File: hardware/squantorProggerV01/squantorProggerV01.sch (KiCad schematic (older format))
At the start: 4 parts

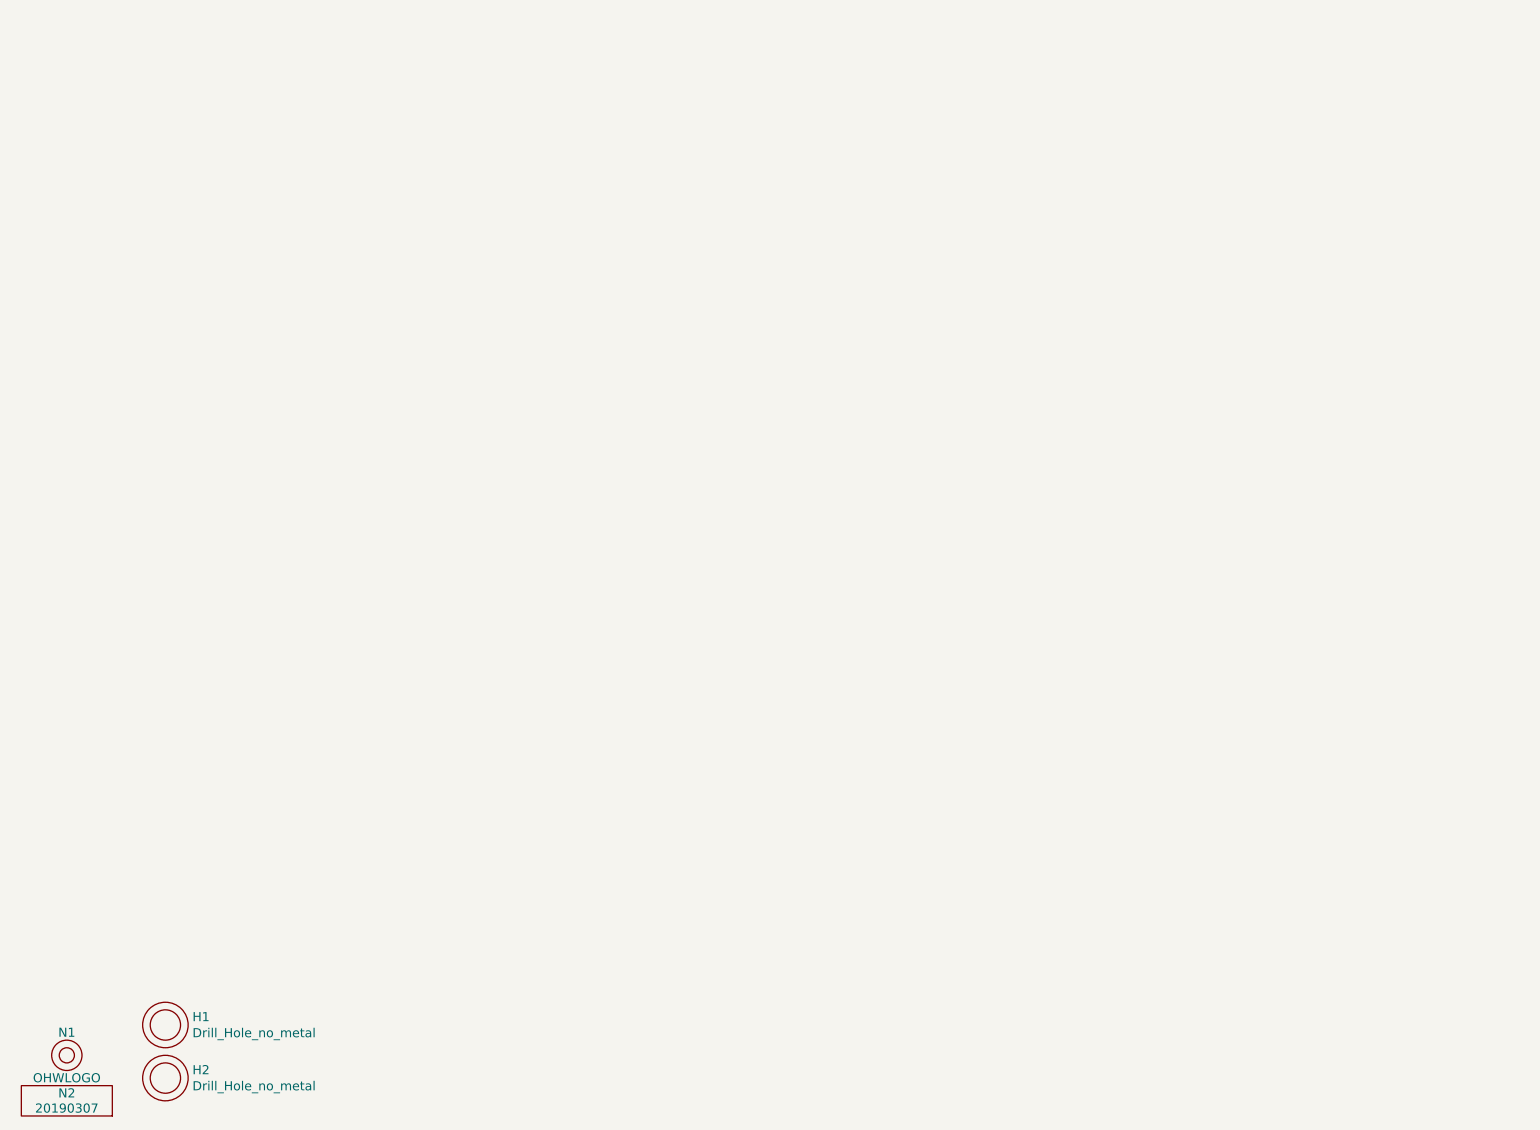
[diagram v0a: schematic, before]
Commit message: placed connectors
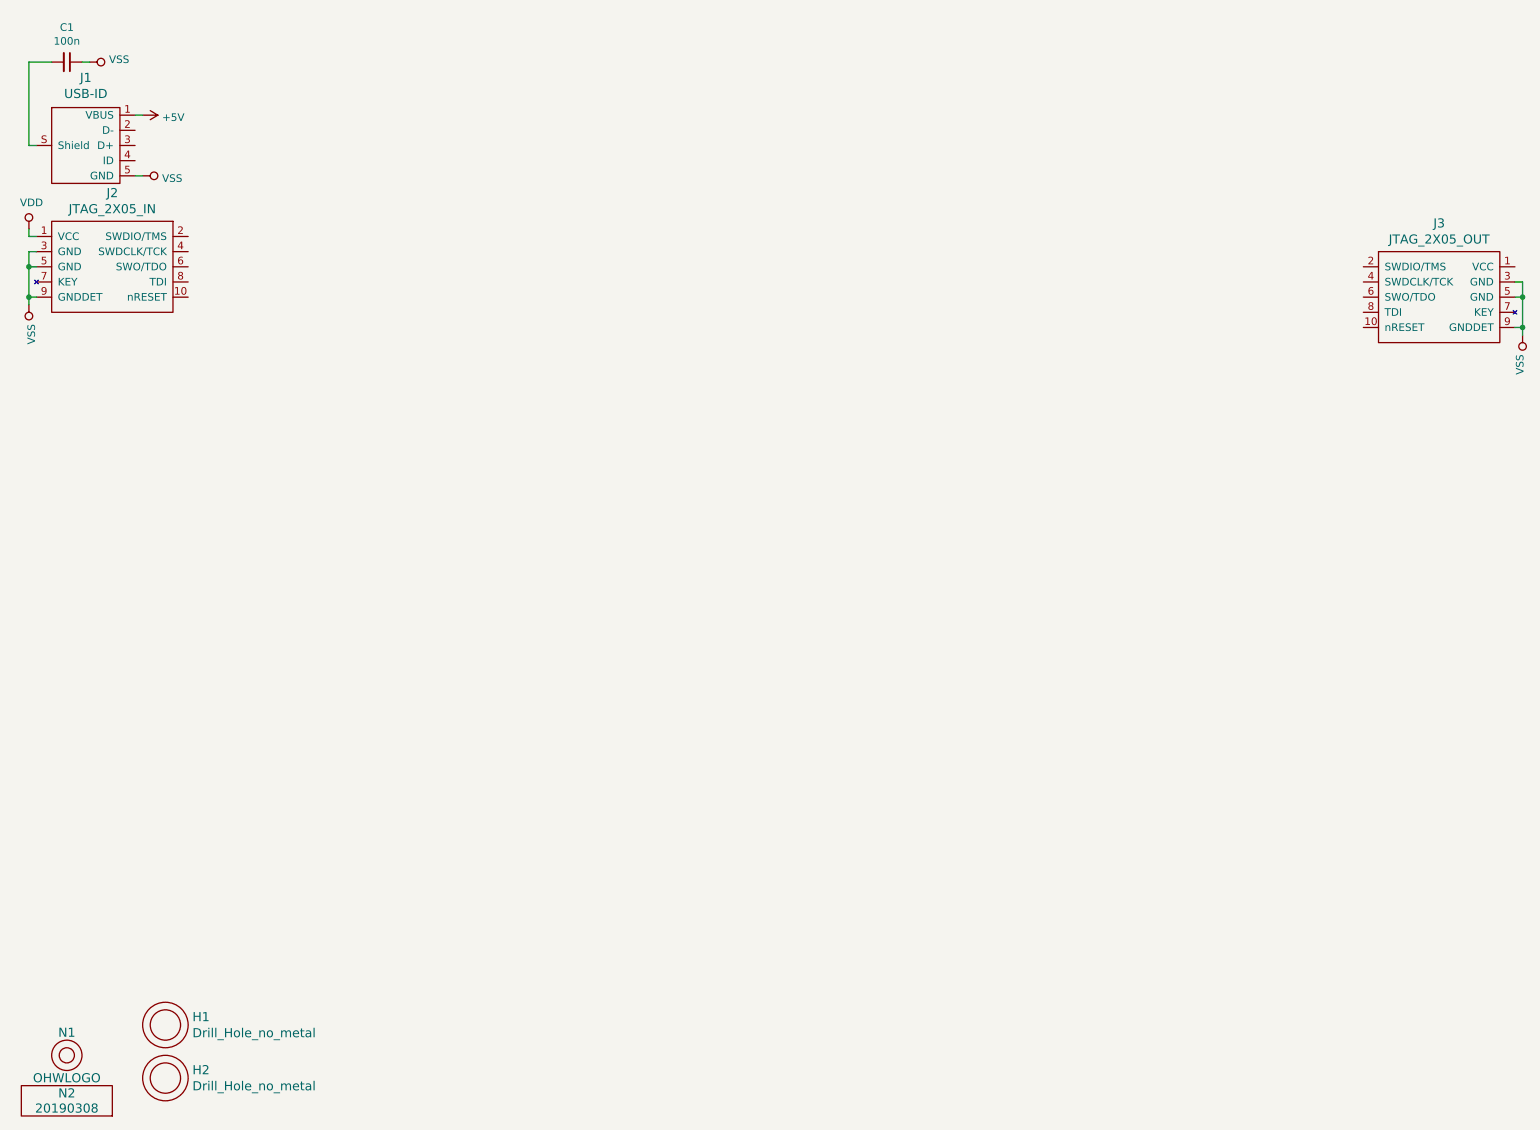
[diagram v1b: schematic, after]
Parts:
- added C1: 100n, SquantorRcl:C_0805, symbol Device:C_Small
- added J1: USB-ID, SquantorUsb:USB-muB-SMD_TH, symbol SquantorUsb:USB-ID
- added J2: JTAG_2X05_IN, SquantorConnectors:Header-0127-2X05-H006, symbol SquantorConnectors:JTAG_2X05_IN
- added J3: JTAG_2X05_OUT, SquantorConnectors:Header-Shr-0127-2X05-H006, symbol SquantorConnectors:JTAG_2X05_OUT
- N2: value 20190307 -> 20190308
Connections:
- new net: C1.2, J1.S (Shield)
- new net +5V: J1.1 (VBUS)
- new net VDD: J2.1 (VCC)
- new net VSS: C1.1, J1.5 (GND), J2.3 (GND), J2.5 (GND), J2.9 (GNDDET), J3.3 (GND), J3.5 (GND), J3.9 (GNDDET)
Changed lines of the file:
@@
 EESchema Schematic File Version 4
-LIBS:Hammond_1551M_OSH2layer-cache
+LIBS:squantorProggerV01-cache
 EELAYER 26 0
 EELAYER END
@@
 P 850 7700
 F 0 "N2" H 850 7800 60  0000 C CNN
-F 1 "20190307" H 850 7700 60  0000 C CNN
+F 1 "20190308" H 850 7700 60  0000 C CNN
 F 2 "SquantorLabels:Label_version" H 850 7700 60  0001 C CNN
 F 3 "" H 850 7700 60  0001 C CNN
@@
 	1    0    0    -1
 $EndComp
+$Comp
+L SquantorUsb:USB-ID J1
+U 1 1 5C82E08A
+P 950 1350
+F 0 "J1" H 975 1797 60  0000 C CNN
+F 1 "USB-ID" H 975 1691 60  0000 C CNN
+F 2 "SquantorUsb:USB-muB-SMD_TH" H 1100 1400 60  0001 C CNN
+F 3 "" H 1100 1400 60  0001 C CNN
+	1    950  1350
+	1    0    0    -1
+$EndComp
+$Comp
+L SquantorConnectors:JTAG_2X05_IN J2
+U 1 1 5C82F4B4
+P 1150 2150
+F 0 "J2" H 1150 2637 60  0000 C CNN
+F 1 "JTAG_2X05_IN" H 1150 2531 60  0000 C CNN
+F 2 "SquantorConnectors:Header-0127-2X05-H006" H 1150 2300 60  0001 C CNN
+F 3 "" H 1150 2300 60  0001 C CNN
+	1    1150 2150
+	-1   0    0    -1
+$EndComp
+$Comp
+L SquantorConnectors:JTAG_2X05_OUT J3
+U 1 1 5C82F5E3
+P 9900 2350
+F 0 "J3" H 9900 2837 60  0000 C CNN
+F 1 "JTAG_2X05_OUT" H 9900 2731 60  0000 C CNN
+F 2 "SquantorConnectors:Header-Shr-0127-2X05-H006" H 9900 2500 60  0001 C CNN
+F 3 "" H 9900 2500 60  0001 C CNN
+	1    9900 2350
+	1    0    0    -1
+$EndComp
+$Comp
+L power:VSS #PWR0101
+U 1 1 5C82FAFA
+P 1350 1550
+F 0 "#PWR0101" H 1350 1400 50  0001 C CNN
+F 1 "VSS" V 1367 1678 50  0000 L CNN
+F 2 "" H 1350 1550 50  0001 C CNN
+F 3 "" H 1350 1550 50  0001 C CNN
+	1    1350 1550
+	0    1    1    0
+$EndComp
+$Comp
+L power:VSS #PWR0102
+U 1 1 5C82FB3D
+P 600 2400
+F 0 "#PWR0102" H 600 2250 50  0001 C CNN
+F 1 "VSS" V 617 2528 50  0000 L CNN
+F 2 "" H 600 2400 50  0001 C CNN
+F 3 "" H 600 2400 50  0001 C CNN
+	1    600  2400
+	1    0    0    1
+$EndComp
+$Comp
+L power:VSS #PWR0103
+U 1 1 5C82FB56
+P 10450 2600
+F 0 "#PWR0103" H 10450 2450 50  0001 C CNN
+F 1 "VSS" V 10467 2728 50  0000 L CNN
+F 2 "" H 10450 2600 50  0001 C CNN
+F 3 "" H 10450 2600 50  0001 C CNN
+	1    10450 2600
+	-1   0    0    1
+$EndComp
+Wire Wire Line
+	10400 2250 10450 2250
+Wire Wire Line
+	10450 2250 10450 2350
+Wire Wire Line
+	10450 2350 10450 2550
+Wire Wire Line
+	10450 2550 10400 2550
+Connection ~ 10450 2350
+Wire Wire Line
+	10400 2350 10450 2350
+Wire Wire Line
+	650  2050 600  2050
+Wire Wire Line
+	600  2050 600  2150
+Wire Wire Line
+	650  2150 600  2150
+Connection ~ 600  2150
+Wire Wire Line
+	650  2350 600  2350
+Wire Wire Line
+	600  2350 600  2150
+Wire Wire Line
+	1300 1550 1350 1550
+Wire Wire Line
+	600  2400 600  2350
+Connection ~ 600  2350
+Wire Wire Line
+	10450 2600 10450 2550
+Connection ~ 10450 2550
+Wire Wire Line
+	650  1950 600  1950
+Wire Wire Line
+	600  1950 600  1900
+$Comp
+L Device:C_Small C1
+U 1 1 5C830A08
+P 850 800
+F 0 "C1" V 621 800 50  0000 C CNN
+F 1 "100n" V 712 800 50  0000 C CNN
+F 2 "SquantorRcl:C_0805" H 850 800 50  0001 C CNN
+F 3 "~" H 850 800 50  0001 C CNN
+	1    850  800
+	0    1    1    0
+$EndComp
+$Comp
+L power:VDD #PWR0104
+U 1 1 5C830AEB
+P 600 1900
+F 0 "#PWR0104" H 600 1750 50  0001 C CNN
+F 1 "VDD" H 617 2073 50  0000 C CNN
+F 2 "" H 600 1900 50  0001 C CNN
+F 3 "" H 600 1900 50  0001 C CNN
+	1    600  1900
+	1    0    0    -1
+$EndComp
+$Comp
+L power:VSS #PWR0105
+U 1 1 5C830B0D
+P 1000 800
+F 0 "#PWR0105" H 1000 650 50  0001 C CNN
+F 1 "VSS" V 1017 928 50  0000 L CNN
+F 2 "" H 1000 800 50  0001 C CNN
+F 3 "" H 1000 800 50  0001 C CNN
+	1    1000 800
+	0    1    -1   0
+$EndComp
+Wire Wire Line
+	650  1350 600  1350
+Wire Wire Line
+	600  1350 600  800
+Wire Wire Line
+	600  800  750  800
+Wire Wire Line
+	1000 800  950  800
+$Comp
+L power:+5V #PWR0106
+U 1 1 5C8314E9
+P 1350 1150
+F 0 "#PWR0106" H 1350 1000 50  0001 C CNN
+F 1 "+5V" V 1365 1278 50  0000 L CNN
+F 2 "" H 1350 1150 50  0001 C CNN
+F 3 "" H 1350 1150 50  0001 C CNN
+	1    1350 1150
+	0    1    1    0
+$EndComp
+Wire Wire Line
+	1300 1150 1350 1150
 $EndSCHEMATC

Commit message: newer Pcb library, started usb serial bits
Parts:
- added C?: 1u, SquantorRcl:C_0603, symbol Device:C_Small
- added U?: CH340E, symbol SquantorWCH:CH340E
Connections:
- net +5V: now also U?.7 (VCC)
- net VSS: now also C?.2, U?.3 (GND)
- net USB_D-: now reaches J1.2 (D-)
- net USB_D-: now also U?.2 (UD-)
- net USB_D+: now reaches J1.3 (D+)
- net USB_D+: now also U?.1 (UD+)
- new net: C?.1, U?.10 (V3)
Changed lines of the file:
@@
 Wire Wire Line
 	1300 1150 1350 1150
+$Comp
+L SquantorWCH:CH340E U?
+U 1 1 5C83DAAF
+P 2600 1350
+F 0 "U?" H 2600 1815 50  0000 C CNN
+F 1 "CH340E" H 2600 1724 50  0000 C CNN
+F 2 "" H 2600 1250 50  0001 C CNN
+F 3 "" H 2600 1250 50  0001 C CNN
+	1    2600 1350
+	1    0    0    -1
+$EndComp
+Wire Wire Line
+	1300 1250 1450 1250
+Wire Wire Line
+	1300 1350 1450 1350
+Text Label 1450 1250 0    50   ~ 0
+USB_D-
+Text Label 1450 1350 0    50   ~ 0
+USB_D+
+$Comp
+L power:VSS #PWR?
+U 1 1 5C83E568
+P 2200 1350
+F 0 "#PWR?" H 2200 1200 50  0001 C CNN
+F 1 "VSS" V 2217 1478 50  0000 L CNN
+F 2 "" H 2200 1350 50  0001 C CNN
+F 3 "" H 2200 1350 50  0001 C CNN
+	1    2200 1350
+	0    -1   -1   0
+$EndComp
+$Comp
+L power:+5V #PWR?
+U 1 1 5C83E80B
+P 3000 1450
+F 0 "#PWR?" H 3000 1300 50  0001 C CNN
+F 1 "+5V" V 3015 1578 50  0000 L CNN
+F 2 "" H 3000 1450 50  0001 C CNN
+F 3 "" H 3000 1450 50  0001 C CNN
+	1    3000 1450
+	0    1    1    0
+$EndComp
+$Comp
+L Device:C_Small C?
+U 1 1 5C83E858
+P 2600 750
+F 0 "C?" V 2371 750 50  0000 C CNN
+F 1 "1u" V 2462 750 50  0000 C CNN
+F 2 "SquantorRcl:C_0603" H 2600 750 50  0001 C CNN
+F 3 "~" H 2600 750 50  0001 C CNN
+	1    2600 750
+	0    1    1    0
+$EndComp
+$Comp
+L power:VSS #PWR?
+U 1 1 5C83E8B1
+P 2450 750
+F 0 "#PWR?" H 2450 600 50  0001 C CNN
+F 1 "VSS" V 2467 878 50  0000 L CNN
+F 2 "" H 2450 750 50  0001 C CNN
+F 3 "" H 2450 750 50  0001 C CNN
+	1    2450 750
+	0    -1   -1   0
+$EndComp
+Wire Wire Line
+	2950 1150 3000 1150
+Wire Wire Line
+	3000 1150 3000 750
+Wire Wire Line
+	3000 750  2700 750
+Wire Wire Line
+	2200 1350 2250 1350
+Wire Wire Line
+	2950 1450 3000 1450
+Wire Wire Line
+	2250 1250 2200 1250
+Wire Wire Line
+	2250 1150 2200 1150
+Text Label 2200 1150 2    50   ~ 0
+USB_D+
+Text Label 2200 1250 2    50   ~ 0
+USB_D-
+Wire Wire Line
+	2500 750  2450 750
 $EndSCHEMATC

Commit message: cleanup of obsolete parts
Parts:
- removed C?: 1u, SquantorRcl:C_0603, symbol Device:C_Small
- removed U?: CH340E, symbol SquantorWCH:CH340E
- J1: symbol SquantorUsb:USB-ID -> squantorProggerV01-rescue:USB-ID-SquantorUsb
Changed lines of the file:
@@
 EESchema Schematic File Version 4
 LIBS:squantorProggerV01-cache
-EELAYER 26 0
+EELAYER 29 0
 EELAYER END
 $Descr A4 11693 8268
@@
 $EndComp
 $Comp
-L SquantorUsb:USB-ID J1
+L squantorProggerV01-rescue:USB-ID-SquantorUsb J1
 U 1 1 5C82E08A
 P 950 1350
@@
 Wire Wire Line
 	1300 1150 1350 1150
-$Comp
-L SquantorWCH:CH340E U?
-U 1 1 5C83DAAF
-P 2600 1350
-F 0 "U?" H 2600 1815 50  0000 C CNN
-F 1 "CH340E" H 2600 1724 50  0000 C CNN
-F 2 "" H 2600 1250 50  0001 C CNN
-F 3 "" H 2600 1250 50  0001 C CNN
-	1    2600 1350
-	1    0    0    -1
-$EndComp
 Wire Wire Line
 	1300 1250 1450 1250
@@
 Text Label 1450 1350 0    50   ~ 0
 USB_D+
-$Comp
-L power:VSS #PWR?
-U 1 1 5C83E568
-P 2200 1350
-F 0 "#PWR?" H 2200 1200 50  0001 C CNN
-F 1 "VSS" V 2217 1478 50  0000 L CNN
-F 2 "" H 2200 1350 50  0001 C CNN
-F 3 "" H 2200 1350 50  0001 C CNN
-	1    2200 1350
-	0    -1   -1   0
-$EndComp
-$Comp
-L power:+5V #PWR?
-U 1 1 5C83E80B
-P 3000 1450
-F 0 "#PWR?" H 3000 1300 50  0001 C CNN
-F 1 "+5V" V 3015 1578 50  0000 L CNN
-F 2 "" H 3000 1450 50  0001 C CNN
-F 3 "" H 3000 1450 50  0001 C CNN
-	1    3000 1450
-	0    1    1    0
-$EndComp
-$Comp
-L Device:C_Small C?
-U 1 1 5C83E858
-P 2600 750
-F 0 "C?" V 2371 750 50  0000 C CNN
-F 1 "1u" V 2462 750 50  0000 C CNN
-F 2 "SquantorRcl:C_0603" H 2600 750 50  0001 C CNN
-F 3 "~" H 2600 750 50  0001 C CNN
-	1    2600 750
-	0    1    1    0
-$EndComp
-$Comp
-L power:VSS #PWR?
-U 1 1 5C83E8B1
-P 2450 750
-F 0 "#PWR?" H 2450 600 50  0001 C CNN
-F 1 "VSS" V 2467 878 50  0000 L CNN
-F 2 "" H 2450 750 50  0001 C CNN
-F 3 "" H 2450 750 50  0001 C CNN
-	1    2450 750
-	0    -1   -1   0
-$EndComp
-Wire Wire Line
-	2950 1150 3000 1150
-Wire Wire Line
-	3000 1150 3000 750
-Wire Wire Line
-	3000 750  2700 750
-Wire Wire Line
-	2200 1350 2250 1350
-Wire Wire Line
-	2950 1450 3000 1450
-Wire Wire Line
-	2250 1250 2200 1250
-Wire Wire Line
-	2250 1150 2200 1150
-Text Label 2200 1150 2    50   ~ 0
-USB_D+
-Text Label 2200 1250 2    50   ~ 0
-USB_D-
-Wire Wire Line
-	2500 750  2450 750
 $EndSCHEMATC
